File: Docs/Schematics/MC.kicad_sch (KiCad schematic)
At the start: 14 parts, among them J1 SWD, U1 ATSAMD20E18, U2 LD1117S33TR_SOT223

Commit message: Revision 2
Fixes based after sponsor interview.
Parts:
- added C6: 100nF, symbol Device:C_Small
- added C7: 33nF, symbol Device:C_Small
- added C8: 1nF, symbol Device:C_Small
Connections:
- net GND: now also C6.2, C7.2, C8.2
- net VDD: now also C6.1, C7.1, C8.1
- net RESET1: now reaches U1.3 (PA02)
- net WAKE1: now reaches U1.4 (PA03)
- net CHIP_EN: now reaches U1.5 (PA04)
- net XOSCIN: no longer names the net of U1.15 (PA14)
- net XOSCOUT: no longer names the net of U1.16 (PA15)
- no-connect marks 0 -> 9
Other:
- moved on the sheet: C1, C2, L1

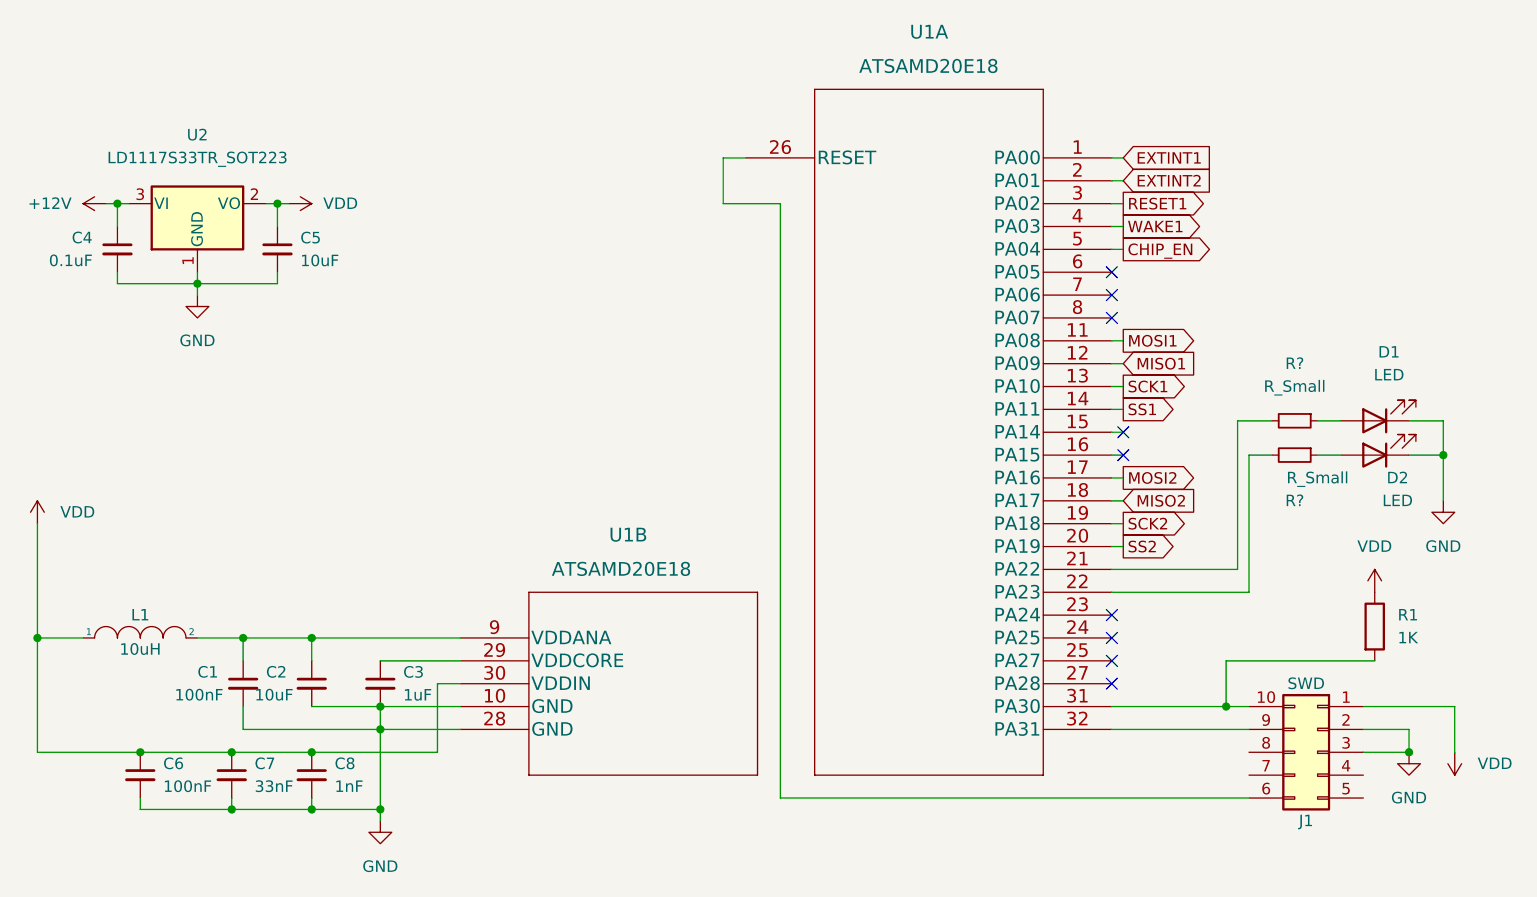
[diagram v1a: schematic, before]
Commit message: Revision 3
Revisions made after meeting with sponsor.
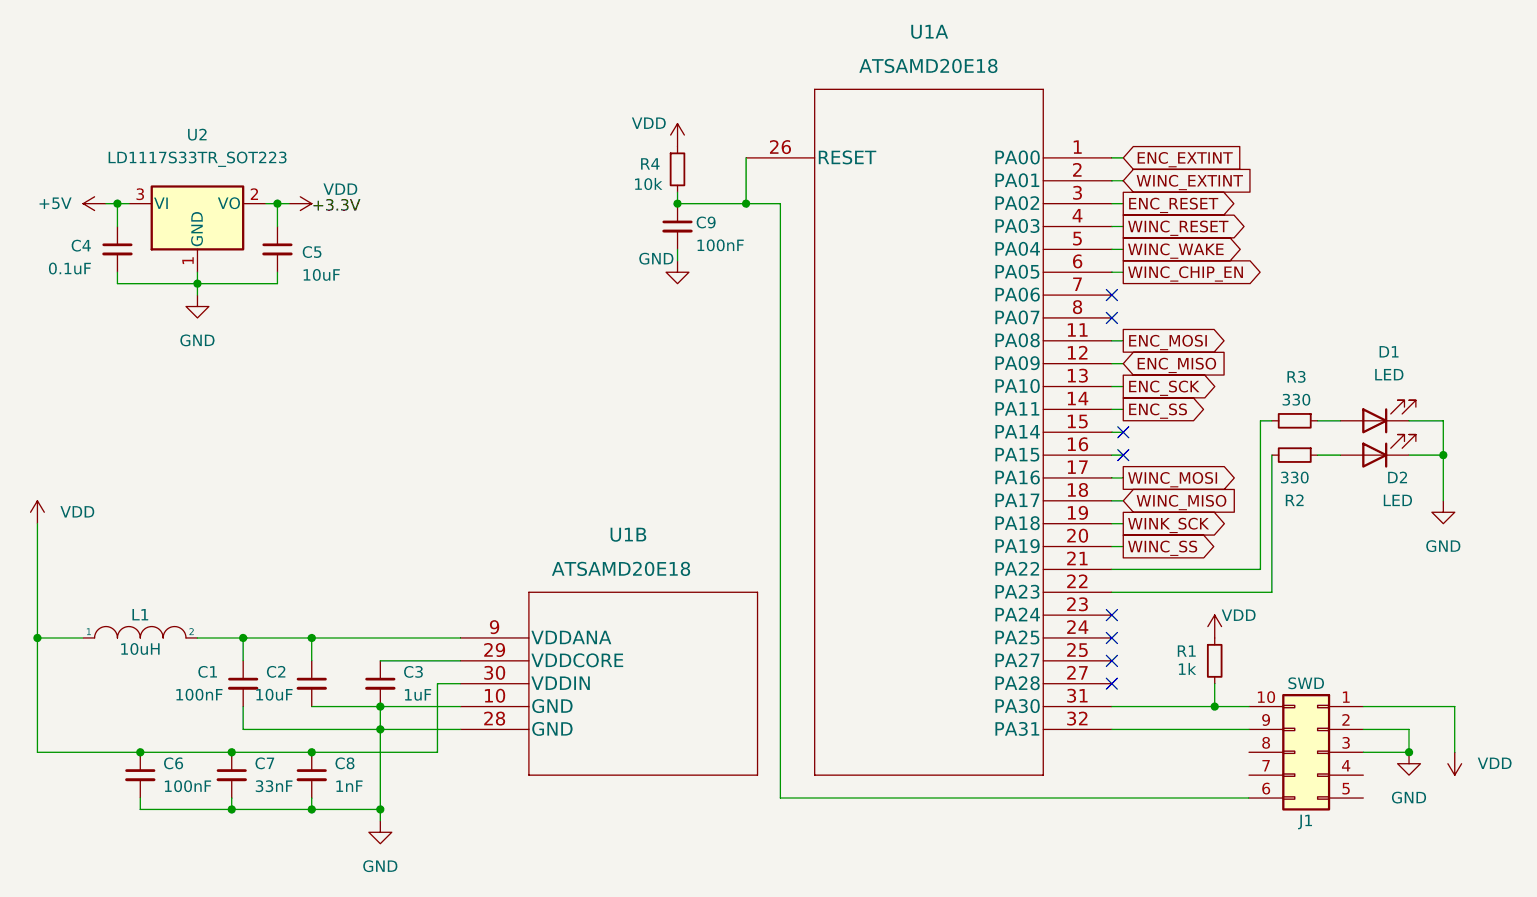
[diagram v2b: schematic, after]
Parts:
- removed R1: 1K, symbol Device:R
- added C9: 100nF, symbol Device:C_Small
- added R1: 1k, symbol Device:R_Small
- added R4: 10k, symbol Device:R_Small
- R2, R3: renamed from R?; value R_Small -> 330
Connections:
- net GND: now also C9.2
- net VDD: now also R1.1, R4.1
- net at J1.6 (Pin_6), U1.26 (RESET): now also C9.1, R4.2
- net at J1.10 (Pin_10), U1.31 (PA30): now also R1.2
- net WINC_CHIP_EN: now reaches U1.6 (PA05)
- net +12V renamed +5V
- net CHIP_EN renamed WINC_WAKE
- net EXTINT1 renamed ENC_EXTINT
- net EXTINT2 renamed WINC_EXTINT
- net MISO1 renamed ENC_MISO
- net MISO2 renamed WINC_MISO
- net MOSI1 renamed ENC_MOSI
- net MOSI2 renamed WINC_MOSI
- net RESET1 renamed ENC_RESET
- net SCK1 renamed ENC_SCK
- net SCK2 renamed WINK_SCK
- net SS1 renamed ENC_SS
- net SS2 renamed WINC_SS
- net WAKE1 renamed WINC_RESET
- no-connect marks 9 -> 8
